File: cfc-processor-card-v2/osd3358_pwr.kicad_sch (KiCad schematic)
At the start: 42 parts, among them Q1 MMBT2907, U10 TLVH431, U4 SN74LVC1G07DCK, U7 OSD3358-512M-BSM

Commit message: Clean up CFC Processor Card from Scott's initial import which was Gerber identical to origianl EAGLE schematic. Interestingly, this version was already changed for the v2 backplane which is great. Align schematic to be more KiCAD like based off of the C3, rename a few things, remove some outdated OPD connections, import sch into pcb, clean up pcb detritus, and import DRU settings. No longer Gerber identicial, but it's now ready for further polishing for fabrication.
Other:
- note removed: "1.2"
- note removed: "OreSat Star Tracker: OSD Power/Misc"
- company: (none) -> Portland State Aerospace Society
- title: (none) -> OreSat CFC Processor Card
- moved on the sheet: C13, C14, C18, D1, Q1, R1, R15, R23, R28, R31, R73, R74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

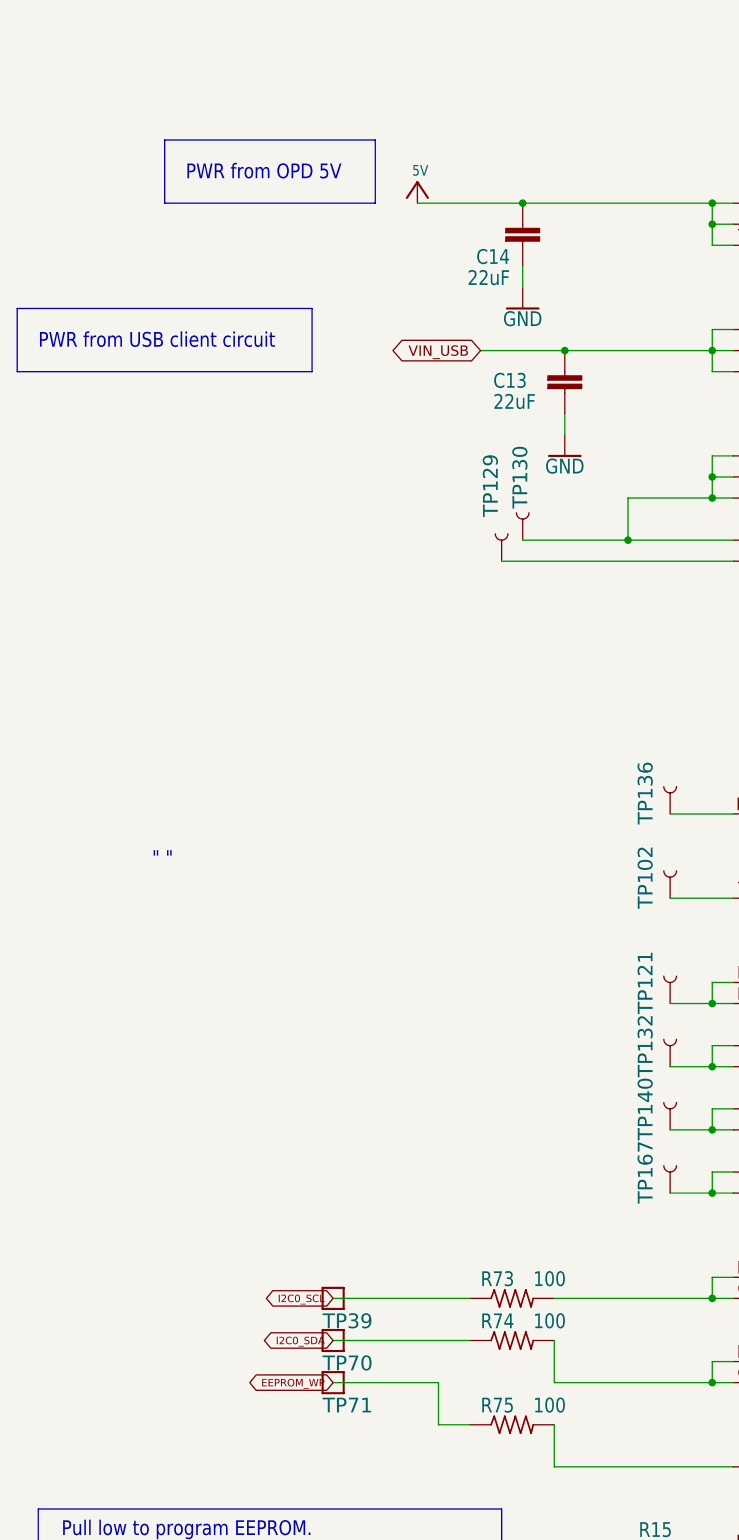
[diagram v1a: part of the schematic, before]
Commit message: Big cleanup - fixed a billion ERCs and DRCs. Switched a bunch of parts over to OreSat parts. Added analog switch on UART so CFC processor can talk serial to C3. Last thing left: clean up passives with new footprints, maybe.
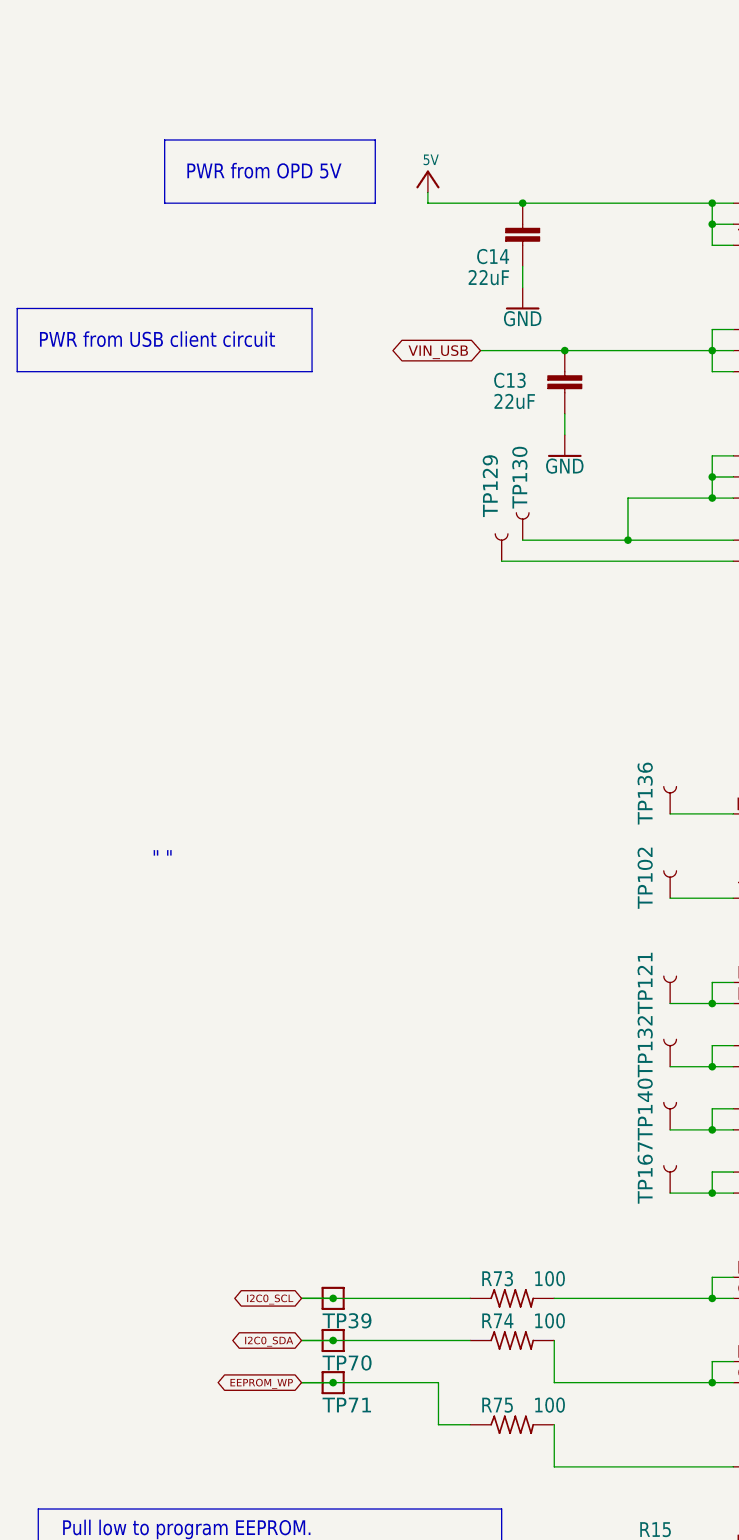
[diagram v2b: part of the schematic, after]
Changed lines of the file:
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@@
 	)
 	(junction
+		(at 63.5 187.96)
+		(diameter 0)
+		(color 0 0 0 0)
+	)
+	(junction
 		(at 109.22 175.26)
 		(diameter 0)
@@
 	)
 	(junction
+		(at 63.5 198.12)
+		(diameter 0)
+		(color 0 0 0 0)
+	)
+	(junction
 		(at 187.96 172.72)
 		(diameter 0)
@@
 	)
 	(junction
+		(at 63.5 193.04)
+		(diameter 0)
+		(color 0 0 0 0)
+	)
+	(junction
 		(at 187.96 124.46)
 		(diameter 0)
@@
 	(wire
 		(pts
+			(xy 74.93 54.61) (xy 74.93 55.88)
+		)
+		(stroke
+			(width 0.1524)
+			(type solid)
+		)
+	)
+	(wire
+		(pts
 			(xy 109.22 55.88) (xy 111.76 55.88)
 		)
@@
 	(wire
 		(pts
+			(xy 63.5 193.04) (xy 59.69 193.04)
+		)
+		(stroke
+			(width 0.1524)
+			(type solid)
+		)
+	)
+	(wire
+		(pts
 			(xy 187.96 175.26) (xy 187.96 172.72)
 		)
@@
 	(wire
 		(pts
-			(xy 109.22 60.96) (xy 109.22 58.42)
+			(xy 63.5 187.96) (xy 59.69 187.96)
 		)
 		(stroke
@@
 	(wire
 		(pts
-			(xy 182.88 132.08) (xy 187.96 132.08)
+			(xy 109.22 60.96) (xy 109.22 58.42)
 		)
 		(stroke
@@
 	(wire
 		(pts
-			(xy 215.9 127) (xy 215.9 106.68)
+			(xy 182.88 132.08) (xy 187.96 132.08)
 		)
 		(stroke
@@
 	(wire
 		(pts
-			(xy 73.66 55.88) (xy 86.36 55.88)
+			(xy 215.9 127) (xy 215.9 106.68)
 		)
 		(stroke
@@
 	(wire
 		(pts
+			(xy 59.69 187.96) (xy 63.5 187.96)
+		)
+		(stroke
+			(width 0)
+			(type default)
+		)
+	)
+	(wire
+		(pts
 			(xy 187.96 124.46) (xy 187.96 121.92)
 		)
@@
 	(wire
 		(pts
+			(xy 74.93 55.88) (xy 86.36 55.88)
+		)
+		(stroke
+			(width 0.1524)
+			(type solid)
+		)
+	)
+	(wire
+		(pts
 			(xy 215.9 152.4) (xy 215.9 137.16)
 		)
@@
 	(wire
 		(pts
+			(xy 63.5 198.12) (xy 76.2 198.12)
+		)
+		(stroke
+			(width 0.1524)
+			(type solid)
+		)
+	)
+	(wire
+		(pts
 			(xy 182.88 139.7) (xy 187.96 139.7)
 		)
@@
 	(wire
 		(pts
+			(xy 59.69 193.04) (xy 63.5 193.04)
+		)
+		(stroke
+			(width 0)
+			(type default)
+		)
+	)
+	(wire
+		(pts
 			(xy 401.32 52.07) (xy 396.24 52.07)
 		)
@@
 	(wire
 		(pts
+			(xy 59.69 198.12) (xy 63.5 198.12)
+		)
+		(stroke
+			(width 0)
+			(type default)
+		)
+	)
+	(wire
+		(pts
 			(xy 182.88 93.98) (xy 187.96 93.98)
 		)
@@
 	(wire
 		(pts
-			(xy 63.5 198.12) (xy 76.2 198.12)
+			(xy 59.69 198.12) (xy 63.5 198.12)
 		)
 		(stroke
@@
 	(global_label "EEPROM_WP"
 		(shape bidirectional)
-		(at 63.5 198.12 180)
+		(at 59.69 198.12 180)
 		(fields_autoplaced yes)
 		(effects
@@
 		)
 		(property "Intersheetrefs" "${INTERSHEET_REFS}"
-			(at 52.7164 198.12 0)
+			(at 48.9064 198.12 0)
 			(effects
 				(font
@@
 				)
 				(justify right)
-				(hide yes)
 			)
 		)
@@
 	(global_label "I2C0_SDA"
 		(shape bidirectional)
-		(at 63.5 193.04 180)
+		(at 59.69 193.04 180)
 		(fields_autoplaced yes)
 		(effects
@@
 		)
 		(property "Intersheetrefs" "${INTERSHEET_REFS}"
-			(at 54.4519 193.04 0)
+			(at 50.6419 193.04 0)
 			(effects
 				(font
@@
 				)
 				(justify right)
-				(hide yes)
 			)
 		)
@@
 	(global_label "I2C0_SCL"
 		(shape bidirectional)
-		(at 63.5 187.96 180)
+		(at 59.69 187.96 180)
 		(fields_autoplaced yes)
 		(effects
@@
 		)
 		(property "Intersheetrefs" "${INTERSHEET_REFS}"
-			(at 54.4942 187.96 0)
+			(at 50.6842 187.96 0)
 			(effects
 				(font
@@
 				)
 				(justify right)
-				(hide yes)
 			)
 		)
@@
 				)
 				(justify right)
-				(hide yes)
 			)
 		)
@@
 	(symbol
 		(lib_id "cfc-card-eagle-import:5V")
-		(at 73.66 53.34 0)
+		(at 74.93 52.07 0)
 		(unit 1)
 		(exclude_from_sim no)
@@
 		(dnp no)
 		(property "Reference" "#3V-26"
-			(at 73.66 53.34 0)
+			(at 74.93 52.07 0)
 			(effects
 				(font
@@
 		)
 		(property "Value" "5V"
-			(at 73.025 52.705 0)
+			(at 74.295 51.435 0)
 			(effects
 				(font
@@
 		)
 		(property "Footprint" ""
-			(at 73.66 53.34 0)
+			(at 74.93 52.07 0)
 			(effects
 				(font
@@
 		)
 		(property "Datasheet" ""
-			(at 73.66 53.34 0)
+			(at 74.93 52.07 0)
 			(effects
 				(font
@@
 		)
 		(property "Description" ""
-			(at 73.66 53.34 0)
+			(at 74.93 52.07 0)
 			(effects
 				(font

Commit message: more trace polishing.
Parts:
- C18, R1, R15, R23, R28, R31, R73, R74, R75: footprint cfc-card:.0603-A -> oresat-passives:0603-C-NOSILK
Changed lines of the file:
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@@
 			)
 		)
-		(property "Footprint" "cfc-card:.0603-A"
+		(property "Footprint" "oresat-passives:0603-C-NOSILK"
 			(at 104.14 218.44 0)
 			(effects
@@
 			)
 		)
-		(property "Footprint" "cfc-card:.0603-A"
+		(property "Footprint" "oresat-passives:0603-C-NOSILK"
 			(at 85.09 187.96 0)
 			(effects
@@
 			)
 		)
-		(property "Footprint" "cfc-card:.0603-A"
+		(property "Footprint" "oresat-passives:0603-C-NOSILK"
 			(at 226.06 200.66 0)
 			(effects
@@
 			)
 		)
-		(property "Footprint" "cfc-card:.0603-A"
+		(property "Footprint" "oresat-passives:0603-C-NOSILK"
 			(at 203.2 81.28 0)
 			(effects
@@
 			)
 		)
-		(property "Footprint" "cfc-card:.0603-A"
+		(property "Footprint" "oresat-passives:0603-C-NOSILK"
 			(at 85.09 203.2 0)
 			(effects
@@
 			)
 		)
-		(property "Footprint" "cfc-card:.0603-A"
+		(property "Footprint" "oresat-passives:0603-C-NOSILK"
 			(at 248.92 139.7 0)
 			(effects
@@
 			)
 		)
-		(property "Footprint" "cfc-card:.0603-A"
+		(property "Footprint" "oresat-passives:0603-C-NOSILK"
 			(at 85.09 193.04 0)
 			(effects
@@
 			)
 		)
-		(property "Footprint" "cfc-card:.0603-A"
+		(property "Footprint" "oresat-passives:0603-C-NOSILK"
 			(at 231.14 139.7 0)
 			(effects
@@
 			)
 		)
-		(property "Footprint" "cfc-card:.0603-A"
+		(property "Footprint" "oresat-passives:0603-C-NOSILK"
 			(at 248.92 114.3 0)
 			(effects

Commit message: Final polish on schematic and PCB. Cleaned up BOM, fixed github issues which were not really issues. Lots of BOM cleanup, with MPNs and DPNs.
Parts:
- removed R73, R74, R75: 100, oresat-passives:0603-C-NOSILK, symbol cfc-card-eagle-import:R-US_0603-A
- removed TP14, TP154, TP156, TP157, TP160, TP166, TP173: TEST-POINT3X4, cfc-card:PAD.03X.04, symbol cfc-card-eagle-import:TEST-POINT3X4
- removed TP39, TP70, TP71: TEST-POINT, cfc-card:2MM-TEST-POINT, symbol cfc-card-eagle-import:TEST-POINT
- removed unit 5 of U7
- removed unit 6 of U7
- added C40: 22u, Capacitor_SMD:C_1210_3225Metric, symbol cfc-card-eagle-import:C-EUC1210
- added C41: 100n, oresat-passives:0603-C-NOSILK, symbol cfc-card-eagle-import:C-EU0603-A
- added J5: Conn_01x04, Connector_PinHeader_2.54mm:PinHeader_1x04_P2.54mm_Vertical, symbol Connector_Generic:Conn_01x04
- added R25: 10k, oresat-passives:0603-C-NOSILK, symbol cfc-card-eagle-import:R-US_0603-A
- C13, C14: value 22uF -> 22u; footprint cfc-card:C1210 -> Capacitor_SMD:C_1210_3225Metric; DIS (none) -> DigiKey; DPN (none) -> 490-GCM32EC71E226KE36KCT-ND; MFR (none) -> Murata Electronics; MPN (none) -> GCM32EC71E226KE36K
- C18: value 0.1uF -> 100n; DIS (none) -> DigiKey; DPN (none) -> 587-3472-1-ND; MFR (none) -> Taiyo Yuden; MPN (none) -> TMK107BJ104KAHT
- D1: footprint cfc-card:LED-0603 -> LED_SMD:LED_0603_1608Metric; symbol cfc-card-eagle-import:LED-GREEN0603 -> Device:LED_Small; DIS (none) -> DigiKey; DPN (none) -> 732-4971-1-ND; MFR (none) -> Wurth; MPN (none) -> 150060GS75000
- Q1: footprint cfc-card:SOT23-BEC -> Package_TO_SOT_SMD:SOT-23; symbol cfc-card-eagle-import:MMBT2907SMD -> Transistor_BJT:Q_PNP_BEC; DIS (none) -> DigiKey; DPN (none) -> 1727-1884-1-ND; MFR (none) -> Nexperia; MPN (none) -> PMBT2907A,235
- R1: DIS (none) -> DigiKey; DPN (none) -> RMCF0603FT1K00CT-ND; MFR (none) -> Stackpole Electronics Inc; MPN (none) -> RMCF0603FT1K00
- R15, R28: DIS (none) -> DigiKey; DPN (none) -> RMCF0603FT10K0CT-ND; MFR (none) -> Stackpole Electronics Inc; MPN (none) -> RMCF0603FT10K0
- R23: DIS (none) -> DigiKey; DPN (none) -> RMCF0603FT499RCT-ND; MFR (none) -> Stackpole Electronics Inc; MPN (none) -> RMCF0603FT499R
- R31: DIS (none) -> DigiKey; DPN (none) -> RMCF0603FT40K2CT-ND; MFR (none) -> Stackpole Electronics Inc; MPN (none) -> RMCF0603FT40K2
- TP102, TP109, TP110, TP121, TP129, TP130, TP132, TP136, TP140, TP161, TP163, TP164, TP165, TP167, TP2, TP3: now left out of the parts list
- U10: footprint cfc-card:SOT23-3 -> Package_TO_SOT_SMD:SOT-23; symbol cfc-card-eagle-import:TLVH431 -> oresat-ics:TLVH431; DIS (none) -> DigiKey; DPN (none) -> 296-17979-1-ND; MFR (none) -> Texas Instruments; MPN (none) -> TLVH431BCDBZT
- U4: value SN74LVC1G07DCK -> SN74AUC1G07DCKR; footprint cfc-card:C70(TI-DCK) -> Package_TO_SOT_SMD:SOT-353_SC-70-5; symbol cfc-card-eagle-import:SN74LVC1G07DCK -> oresat-ics:SN74LVC1G07DCK; DIS (none) -> DigiKey; DPN (none) -> 296-12464-1-ND; MFR (none) -> Texas Instruments; MPN (none) -> SN74AUC1G07DCKR
- U7: value OSD3358-512M-BSM -> OSD3358-1G-ISM; footprint cfc-card:OSD335X-BGA-256 -> oresat-ics:U-Octavo-OSD335X-BGA-256; symbol cfc-card-eagle-import:OSD3358-512M-BSM -> oresat-ics:OSD3358-512M-BSM; DIS (none) -> DigiKey; DPN (none) -> 1676-OSD3358-1G-ISM-ND; MFR (none) -> Octavo Systems; MPN (none) -> OSD3358-1G-ISM
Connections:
- net 3.3V: now also R25.1
- net 3.3VA: now also Q1.2 (E); no longer Q1.E
- net EEPROM_WP: now also U7.M2 (EEPROM_WP), J5.3 (Pin_3)
- net GND: now also D1.1 (K), C40.2, C41.2, J5.4 (Pin_4); no longer D1.C
- net I2C0_SCL: now also U7.C10 (I2C0_SCL), U7.D10 (PMIC_SCL), J5.1 (Pin_1)
- net I2C0_SDA: now also U7.C11 (I2C0_SDA), U7.D11 (PMIC_SDA), J5.2 (Pin_2)
- net VDD: now also C40.1
- net at R1.2: now also D1.2 (A); no longer D1.A
- net at R23.1, U10.2 (K): now also Q1.1 (B); no longer Q1.B
- net N$118: no longer names the net of C18.1, R31.1, TP164.P$1 (1), U10.3 (A), U4.5 (VCC), U7.K11 (SYS_RTC_1P8V@1), U7.L11 (SYS_RTC_1P8V@2)
- net N$118: now also Q1.3 (C); no longer Q1.C
- net RESET# renamed nRESET
- net nRESET: now also C41.1, R25.2
- no-connect marks 3 -> 0
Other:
- note added: "1210"
- note added: "5V Power in (OR'd)"
- note added: "EEPROM Programming Jumper Pull Pin 3 low to write to EEPROM. Use Raspberry Pi Pico board with Circuit Python software to program. Careful with ESD!"
- note added: "Power from Backplane (Vbus via Vbusp) from 5V SPS"
- note added: "Power from Debug connector (USB client)"
- note added: "SYS_VDD1_3P3V is a 3.3V output of the OSD3358. It's generated from an internal TL5209 LDO. Imax = 500 mA, including draw from the OSD3358."
- note added: "SYS_VOUT is the OR of 5V from the bus and VIN_USB. Imax = 500 mA"
- note removed: "PWR from OPD 5V"
- note removed: "PWR from USB client circuit"
- note removed: "Power Management Buffer powered from SYS_RTC_1P8V"
- note removed: "Pull low to program EEPROM. Program EEPROM with below script, using another Pocketbeagle oresat-star-tracker/utils/i2c-program-board-id.py"
- note removed: "SYS_VDD1_3P3V is where system 3.3V power originates, 500mA max,"
- note removed: "SYS_VOUT is where system 5V power originates, 500mA max. This will always be 5V as long as VIN_AC or VIN_USB are used at 5V. However, if VIN_BAT is used with non-5V input, this will reflect that voltage. VIN_BAT will probably be used from the oresat power circuit, so we need to prepare for this case. Likewise, right now the only component using 5V is the USB host circuit"
- moved on the sheet: C18, R1, TP129, TP130, TP3
